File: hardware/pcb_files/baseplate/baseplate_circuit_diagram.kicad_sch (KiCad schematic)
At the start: 9 parts, among them J2 PC Interface?, J3 DATA_OUT1_for_1_Wire_Communic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, J5 UART to TTL Adapter, J6 UART to TTL Adapter Programmer, U1 ATtiny1616-S

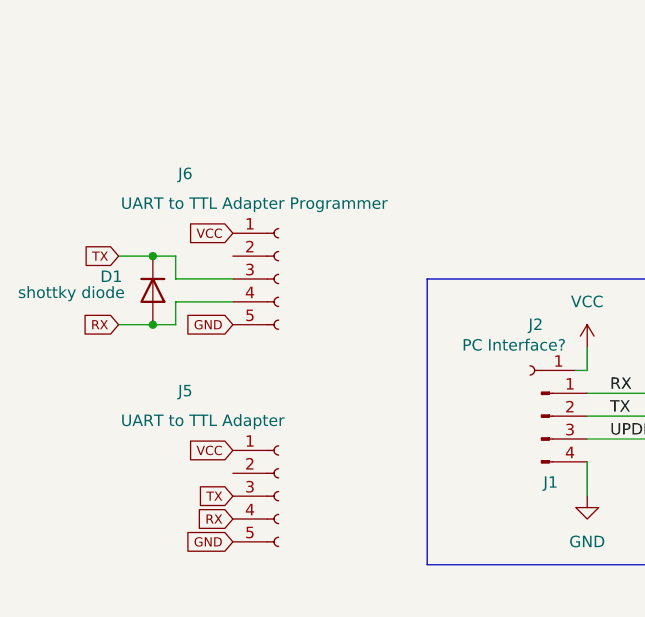
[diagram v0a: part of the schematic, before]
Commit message: debug codes added for debugging baseplate firmware
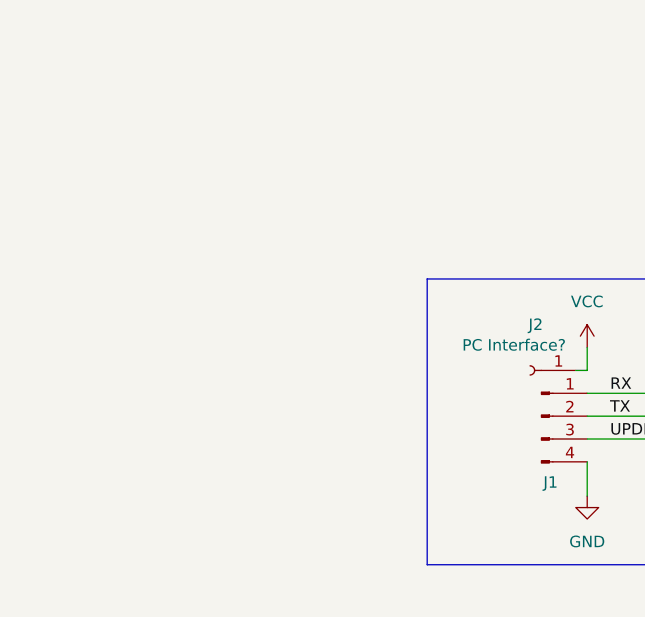
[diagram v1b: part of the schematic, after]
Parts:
- removed D1: shottky diode, Diode_THT:D_DO-35_SOD27_P7.62mm_Horizontal, symbol Diode:1N914
- removed J5: UART to TTL Adapter, symbol Connector:Conn_01x05_Socket
- removed J6: UART to TTL Adapter Programmer, symbol Connector:Conn_01x05_Socket
